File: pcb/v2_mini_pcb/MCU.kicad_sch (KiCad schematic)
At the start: 13 parts, among them SW1 SW_Push, SW2 SW_Push

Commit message: update pcb issues
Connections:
- net CHG_PG: now reaches U2.51 (GPIO40)
- no-connect marks 16 -> 15
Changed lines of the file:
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@@
-	)
-	(no_connect
-		(at 165.1 156.21)
 	)
 	(no_connect
@@
 	)
 	(bus_entry
+		(at 55.88 57.15)
+		(size -2.54 2.54)
+		(stroke
+			(width 0)
+			(type default)
+		)
+	)
+	(bus_entry
 		(at 119.38 62.23)
 		(size -2.54 2.54)
@@
 		)
 	)
+	(bus
+		(pts
+			(xy 55.88 52.07) (xy 55.88 57.15)
+		)
+		(stroke
+			(width 0)
+			(type default)
+		)
+	)
 	(wire
 		(pts
@@
 	(wire
 		(pts
+			(xy 53.34 59.69) (xy 38.1 59.69)
+		)
+		(stroke
+			(width 0)
+			(type default)
+		)
+	)
+	(wire
+		(pts
 			(xy 43.18 105.41) (xy 41.91 105.41)
 		)
@@
 		(pts
 			(xy 116.84 69.85) (xy 101.6 69.85)
+		)
+		(stroke
+			(width 0)
+			(type default)
+		)
+	)
+	(wire
+		(pts
+			(xy 165.1 156.21) (xy 181.61 156.21)
 		)
 		(stroke
@@
 		)
 	)
+	(label "CHG_PG"
+		(at 38.1 59.69 0)
+		(effects
+			(font
+				(size 1.27 1.27)
+			)
+			(justify left bottom)
+		)
+	)
 	(label "LCD_RN"
 		(at 194.31 34.29 0)
@@
 		(effects
 			(font
+				(size 1.27 1.27)
+			)
+			(justify right bottom)
+		)
+	)
+	(label "CHG_PG"
+		(at 181.61 156.21 180)
+		(effects
+			(font

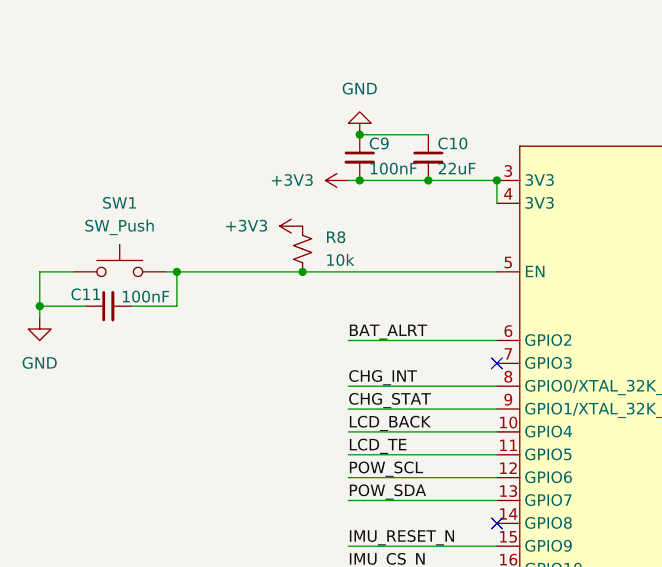
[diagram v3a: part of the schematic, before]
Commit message: ground to imu pins
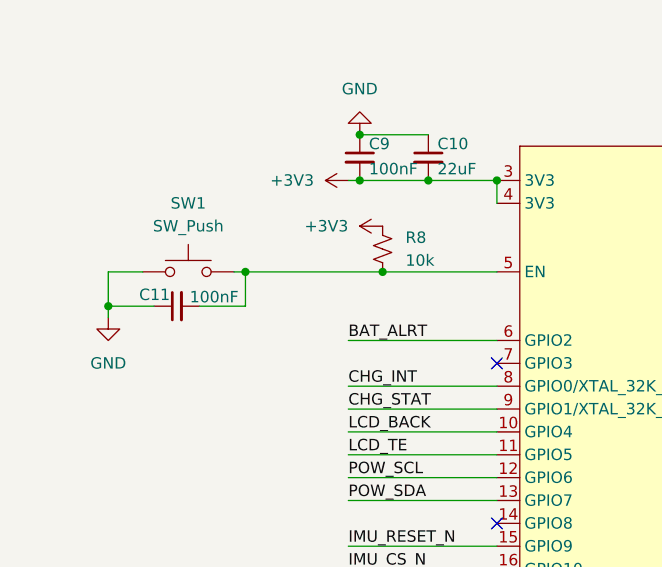
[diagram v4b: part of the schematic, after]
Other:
- moved on the sheet: C11, R8, SW1
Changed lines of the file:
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@@
 	(paper "A3")
 	(junction
-		(at 27.94 109.22)
+		(at 66.04 105.41)
 		(diameter 0)
 		(color 0 0 0 0)
 	)
 	(junction
-		(at 71.12 95.25)
+		(at 35.56 109.22)
 		(diameter 0)
 		(color 0 0 0 0)
 	)
 	(junction
-		(at 63.5 95.25)
+		(at 71.12 95.25)
 		(diameter 0)
 		(color 0 0 0 0)
 	)
 	(junction
-		(at 172.72 100.33)
+		(at 63.5 95.25)
 		(diameter 0)
 		(color 0 0 0 0)
 	)
 	(junction
-		(at 57.15 105.41)
+		(at 172.72 100.33)
 		(diameter 0)
 		(color 0 0 0 0)
@@
 	)
 	(junction
-		(at 43.18 105.41)
+		(at 50.8 105.41)
 		(diameter 0)
 		(color 0 0 0 0)
@@
 	(wire
 		(pts
-			(xy 27.94 109.22) (xy 27.94 105.41)
+			(xy 35.56 109.22) (xy 35.56 105.41)
 		)
 		(stroke
@@
 	(wire
 		(pts
-			(xy 43.18 109.22) (xy 43.18 105.41)
+			(xy 50.8 109.22) (xy 50.8 105.41)
 		)
 		(stroke
@@
 	(wire
 		(pts
-			(xy 43.18 105.41) (xy 57.15 105.41)
+			(xy 50.8 105.41) (xy 66.04 105.41)
 		)
 		(stroke
@@
 	(wire
 		(pts
-			(xy 27.94 110.49) (xy 27.94 109.22)
+			(xy 35.56 110.49) (xy 35.56 109.22)
 		)
 		(stroke
@@
 	(wire
 		(pts
-			(xy 38.1 109.22) (xy 43.18 109.22)
+			(xy 45.72 109.22) (xy 50.8 109.22)
 		)
 		(stroke
@@
 	(wire
 		(pts
-			(xy 43.18 105.41) (xy 41.91 105.41)
+			(xy 50.8 105.41) (xy 49.53 105.41)
 		)
 		(stroke
@@
 	(wire
 		(pts
-			(xy 27.94 109.22) (xy 33.02 109.22)
+			(xy 35.56 109.22) (xy 40.64 109.22)
 		)
 		(stroke
@@
 	(wire
 		(pts
-			(xy 27.94 105.41) (xy 31.75 105.41)
+			(xy 35.56 105.41) (xy 39.37 105.41)
 		)
 		(stroke
@@
 	(wire
 		(pts
-			(xy 86.36 44.45) (xy 71.12 44.45)
+			(xy 66.04 105.41) (xy 78.74 105.41)
 		)
 		(stroke
@@
 	(wire
 		(pts
-			(xy 132.08 49.53) (xy 152.4 49.53)
+			(xy 86.36 44.45) (xy 71.12 44.45)
 		)
 		(stroke
@@
 	(wire
 		(pts
-			(xy 62.23 118.11) (xy 78.74 118.11)
+			(xy 132.08 49.53) (xy 152.4 49.53)
 		)
 		(stroke
@@
 	(wire
 		(pts
-			(xy 57.15 105.41) (xy 78.74 105.41)
+			(xy 62.23 118.11) (xy 78.74 118.11)
 		)
 		(stroke
@@
 	(symbol
 		(lib_id "power:GND")
-		(at 27.94 110.49 0)
+		(at 35.56 110.49 0)
 		(unit 1)
 		(body_style 1)
@@
 		(fields_autoplaced yes)
 		(property "Reference" "#PWR059"
-			(at 27.94 116.84 0)
+			(at 35.56 116.84 0)
 			(hide yes)
 			(show_name no)
@@
 		)
 		(property "Value" "GND"
-			(at 27.94 115.57 0)
+			(at 35.56 115.57 0)
 			(show_name no)
 			(do_not_autoplace no)
@@
 		)
 		(property "Footprint" ""
-			(at 27.94 110.49 0)
+			(at 35.56 110.49 0)
 			(hide yes)
 			(show_name no)
@@
 		)
 		(property "Datasheet" ""
-			(at 27.94 110.49 0)
+			(at 35.56 110.49 0)
 			(hide yes)
 			(show_name no)
@@
 		)
 		(property "Description" "Power symbol creates a global label with name \"GND\" , ground"
-			(at 27.94 110.49 0)
+			(at 35.56 110.49 0)
 			(hide yes)
 			(show_name no)
@@
 	(symbol
 		(lib_id "Device:C_Small")
-		(at 35.56 109.22 90)
+		(at 43.18 109.22 90)
 		(unit 1)
 		(body_style 1)
@@
 		(dnp no)
 		(property "Reference" "C11"
-			(at 34.798 107.95 90)
+			(at 42.418 107.95 90)
 			(show_name no)
 			(do_not_autoplace no)
@@
 		)
 		(property "Value" "100nF"
-			(at 42.418 108.204 90)
+			(at 50.038 108.204 90)
 			(show_name no)
 			(do_not_autoplace no)
@@
 		)
 		(property "Footprint" ""
-			(at 35.56 109.22 0)
+			(at 43.18 109.22 0)
 			(hide yes)
 			(show_name no)
@@
 		)
 		(property "Datasheet" ""
-			(at 35.56 109.22 0)
+			(at 43.18 109.22 0)
 			(hide yes)
 			(show_name no)
@@
 		)
 		(property "Description" "Unpolarized capacitor, small symbol"
-			(at 35.56 109.22 0)
+			(at 43.18 109.22 0)
 			(hide yes)
 			(show_name no)
@@
 	(symbol
 		(lib_id "Switch:SW_Push")
-		(at 36.83 105.41 0)
+		(at 44.45 105.41 0)
 		(unit 1)
 		(body_style 1)
@@
 		(fields_autoplaced yes)
 		(property "Reference" "SW1"
-			(at 36.83 97.79 0)
+			(at 44.45 97.79 0)
 			(show_name no)
 			(do_not_autoplace no)
@@
 		)
 		(property "Value" "SW_Push"
-			(at 36.83 100.33 0)
+			(at 44.45 100.33 0)
 			(show_name no)
 			(do_not_autoplace no)
@@
 		)
 		(property "Footprint" ""
-			(at 36.83 100.33 0)
+			(at 44.45 100.33 0)
 			(hide yes)
 			(show_name no)
@@
 		)
 		(property "Datasheet" ""
-			(at 36.83 100.33 0)
+			(at 44.45 100.33 0)
 			(hide yes)
 			(show_name no)
@@
 		)
 		(property "Description" "Push button switch, generic, two pins"
-			(at 36.83 105.41 0)
+			(at 44.45 105.41 0)
 			(hide yes)
 			(show_name no)
@@
 	(symbol
 		(lib_id "power:+3V3")
-		(at 57.15 100.33 90)
+		(at 66.04 100.33 90)
 		(unit 1)
 		(body_style 1)
@@
 		(fields_autoplaced yes)
 		(property "Reference" "#PWR058"
-			(at 60.96 100.33 0)
+			(at 69.85 100.33 0)
 			(hide yes)
 			(show_name no)
@@
 		)
 		(property "Value" "+3V3"
-			(at 53.34 100.3299 90)
+			(at 62.23 100.3299 90)
 			(show_name no)
 			(do_not_autoplace no)
@@
 		)
 		(property "Footprint" ""
-			(at 57.15 100.33 0)
+			(at 66.04 100.33 0)
 			(hide yes)
 			(show_name no)
@@
 		)
 		(property "Datasheet" ""
-			(at 57.15 100.33 0)
+			(at 66.04 100.33 0)
 			(hide yes)
 			(show_name no)
@@
 		)
 		(property "Description" "Power symbol creates a global label with name \"+3V3\""
-			(at 57.15 100.33 0)
+			(at 66.04 100.33 0)
 			(hide yes)
 			(show_name no)
@@
 	(symbol
 		(lib_id "Device:R_Small_US")
-		(at 57.15 102.87 0)
+		(at 66.04 102.87 0)
 		(unit 1)
 		(body_style 1)
@@
 		(fields_autoplaced yes)
 		(property "Reference" "R8"
-			(at 59.69 101.5999 0)
+			(at 68.58 101.5999 0)
 			(show_name no)
 			(do_not_autoplace no)
@@
 		)
 		(property "Value" "10k"
-			(at 59.69 104.1399 0)
+			(at 68.58 104.1399 0)
 			(show_name no)
 			(do_not_autoplace no)
@@
 		)
 		(property "Footprint" ""
-			(at 57.15 102.87 0)
+			(at 66.04 102.87 0)
 			(hide yes)
 			(show_name no)
@@
 		)
 		(property "Datasheet" ""
-			(at 57.15 102.87 0)
+			(at 66.04 102.87 0)
 			(hide yes)
 			(show_name no)
@@
 		)
 		(property "Description" "Resistor, small US symbol"
-			(at 57.15 102.87 0)
+			(at 66.04 102.87 0)
 			(hide yes)
 			(show_name no)

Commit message: add mpn and footprints for some
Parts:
- added C12, C24: DNP, Capacitor_SMD:C_01005_0402Metric, symbol Device:C_Small
- added J5: TC2030, Connector:Tag-Connect_TC2030-IDC-NL_2x03_P1.27mm_Vertical, symbol Connector:TC2030
- added R30, R31: 22, symbol Device:R_Small_US
- C10: footprint (none) -> Capacitor_SMD:C_0201_0603Metric; MPN (none) -> CL10A226MQ8NRNC
- C11, C9: footprint (none) -> Capacitor_SMD:C_01005_0402Metric; MPN (none) -> CL05B104KB54PNC
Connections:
- net +3V3: now also J5.1
- net GND: now also C12.2, C24.2, J5.5
- net at R17.1: now also U2.41 (USB_DM); no longer U2.43 (GPIO34)
- net at U2.42 (GPIO33): now also R30.1; no longer R10.1
- net at U2.40 (USB_DP): now also R10.1
- net USB_VBUS_S: now reaches U2.44 (GPIO35)
- new net: R31.1, U2.43 (GPIO34)
- new net JTAG_DN: C24.1, J5.3, R30.2
- new net JTAG_DP: C12.1, J5.4, R31.2
- no-connect marks 15 -> 14
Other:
- moved on the sheet: R10, R17

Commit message: finish off mpn and footprints
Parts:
- C10: footprint Capacitor_SMD:C_0201_0603Metric -> Capacitor_SMD:C_0805_2012Metric; MPN CL10A226MQ8NRNC -> GRM21BR61A226ME44L
- C11, C9: footprint Capacitor_SMD:C_01005_0402Metric -> Capacitor_SMD:C_0402_1005Metric; MPN CL05B104KB54PNC -> GRM155R71C104KA88D
- C12, C24: footprint Capacitor_SMD:C_01005_0402Metric -> Capacitor_SMD:C_0402_1005Metric; MPN CL05A105KA5NQNC -> DNP
- J5: MPN (none) -> TC2030-IDC-NL (mating cable)
- R10, R17, R30, R31: footprint (none) -> Resistor_SMD:R_0402_1005Metric; MPN (none) -> 0402WGF220JTCE
- R18: footprint (none) -> Resistor_SMD:R_0402_1005Metric; MPN (none) -> RC0402FR-07499RL
- R8, R9: footprint (none) -> Resistor_SMD:R_0402_1005Metric; MPN (none) -> 0402WGF1002TCE
- SW1, SW2: footprint (none) -> Button_Switch_SMD:SW_SPST_B3U-1000P; MPN (none) -> B3U-1000P
- TP1, TP2: footprint (none) -> TestPoint:TestPoint_Pad_D1.0mm; MPN (none) -> N/A (PCB test pad)
- U2: footprint PCM_Espressif:ESP32-S31-WROOM-3 -> all:ESP32-S31-WROOM-3; MPN (none) -> ESP32-S31-WROOM-3-N16R16V
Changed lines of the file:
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@@
 			)
 		)
-		(property "Footprint" "Capacitor_SMD:C_01005_0402Metric"
+		(property "Footprint" "Capacitor_SMD:C_0402_1005Metric"
 			(at 340.36 88.9 0)
 			(hide yes)
@@
 			)
 		)
-		(property "MPN" "CL05A105KA5NQNC"
+		(property "MPN" "DNP"
 			(at 340.36 88.9 0)
 			(hide yes)
@@
 			)
 		)
-		(property "Footprint" "Capacitor_SMD:C_01005_0402Metric"
+		(property "Footprint" "Capacitor_SMD:C_0402_1005Metric"
 			(at 43.18 109.22 0)
 			(hide yes)
@@
 			)
 		)
-		(property "MPN" "CL05B104KB54PNC"
+		(property "MPN" "GRM155R71C104KA88D"
 			(at 43.18 109.22 90)
 			(hide yes)
@@
 			)
 		)
-		(property "Footprint" "Capacitor_SMD:C_0201_0603Metric"
+		(property "Footprint" "Capacitor_SMD:C_0805_2012Metric"
 			(at 71.12 92.71 0)
 			(hide yes)
@@
 			)
 		)
-		(property "MPN" "CL10A226MQ8NRNC"
+		(property "MPN" "GRM21BR61A226ME44L"
 			(at 71.12 92.71 0)
 			(hide yes)
@@
 			)
 		)
-		(property "Footprint" ""
+		(property "Footprint" "Button_Switch_SMD:SW_SPST_B3U-1000P"
 			(at 44.45 100.33 0)
 			(hide yes)
@@
 			)
 		)
-		(property "MPN" ""
+		(property "MPN" "B3U-1000P"
 			(at 44.45 105.41 0)
 			(hide yes)
@@
 			)
 		)
-		(property "Footprint" ""
+		(property "Footprint" "Resistor_SMD:R_0402_1005Metric"
 			(at 124.46 180.34 0)
 			(hide yes)
@@
 			)
 		)
-		(property "MPN" ""
+		(property "MPN" "0402WGF220JTCE"
 			(at 124.46 180.34 90)
 			(hide yes)
@@
 			)
 		)
-		(property "MPN" ""
+		(property "MPN" "TC2030-IDC-NL (mating cable)"
 			(at 323.85 86.36 0)
 			(hide yes)
@@
 			)
 		)
-		(property "Footprint" ""
+		(property "Footprint" "Resistor_SMD:R_0402_1005Metric"
 			(at 129.54 180.34 0)
 			(hide yes)
@@
 			)
 		)
-		(property "MPN" ""
+		(property "MPN" "0402WGF220JTCE"
 			(at 129.54 180.34 90)
 			(hide yes)
@@
 			)
 		)
-		(property "Footprint" ""
+		(property "Footprint" "Resistor_SMD:R_0402_1005Metric"
 			(at 127 180.34 0)
 			(hide yes)
@@
 			)
 		)
-		(property "MPN" ""
+		(property "MPN" "0402WGF220JTCE"
 			(at 127 180.34 90)
 			(hide yes)
@@
 			)
 		)
-		(property "Footprint" ""
+		(property "Footprint" "Resistor_SMD:R_0402_1005Metric"
 			(at 171.45 110.49 0)
 			(hide yes)
@@
 			)
 		)
-		(property "MPN" ""
+		(property "MPN" "RC0402FR-07499RL"
 			(at 171.45 110.49 90)
 			(hide yes)
@@
 			)
 		)
-		(property "Footprint" ""
+		(property "Footprint" "Resistor_SMD:R_0402_1005Metric"
 			(at 172.72 97.79 0)
 			(hide yes)
@@
 			)
 		)
-		(property "MPN" ""
+		(property "MPN" "0402WGF1002TCE"
 			(at 172.72 97.79 0)
 			(hide yes)
@@
 			)
 		)
-		(property "Footprint" "Capacitor_SMD:C_01005_0402Metric"
+		(property "Footprint" "Capacitor_SMD:C_0402_1005Metric"
 			(at 306.07 88.9 0)
 			(hide yes)
@@
 			)
 		)
-		(property "MPN" "CL05A105KA5NQNC"
+		(property "MPN" "DNP"
 			(at 306.07 88.9 0)
 			(hide yes)
@@
 			)
 		)
-		(property "Footprint" ""
+		(property "Footprint" "Button_Switch_SMD:SW_SPST_B3U-1000P"
 			(at 189.23 95.25 0)
 			(hide yes)
@@
 			)
 		)
-		(property "MPN" ""
+		(property "MPN" "B3U-1000P"
 			(at 189.23 100.33 0)
 			(hide yes)
@@
 			)
 		)
-		(property "Footprint" ""
+		(property "Footprint" "Resistor_SMD:R_0402_1005Metric"
 			(at 121.92 180.34 0)
 			(hide yes)
@@
 			)
 		)
-		(property "MPN" ""
+		(property "MPN" "0402WGF220JTCE"
 			(at 121.92 180.34 90)
 			(hide yes)
@@
 			)
 		)
-		(property "Footprint" ""
+		(property "Footprint" "Resistor_SMD:R_0402_1005Metric"
 			(at 66.04 102.87 0)
 			(hide yes)
@@
 			)
 		)
-		(property "MPN" ""
+		(property "MPN" "0402WGF1002TCE"
 			(at 66.04 102.87 0)
 			(hide yes)
@@
 			)
 		)
-		(property "Footprint" "Capacitor_SMD:C_01005_0402Metric"
+		(property "Footprint" "Capacitor_SMD:C_0402_1005Metric"
 			(at 63.5 92.71 0)
 			(hide yes)
@@
 			)
 		)
-		(property "MPN" "CL05B104KB54PNC"
+		(property "MPN" "GRM155R71C104KA88D"
 			(at 63.5 92.71 0)
 			(hide yes)
@@
 			)
 		)
-		(property "Footprint" ""
+		(property "Footprint" "TestPoint:TestPoint_Pad_D1.0mm"
 			(at 179.07 113.03 0)
 			(hide yes)
@@
 			)
 		)
-		(property "MPN" ""
+		(property "MPN" "N/A (PCB test pad)"
 			(at 179.07 107.95 90)
 			(hide yes)
@@
 			)
 		)
-		(property "Footprint" "PCM_Espressif:ESP32-S31-WROOM-3"
+		(property "Footprint" "all:ESP32-S31-WROOM-3"
 			(at 122.174 187.96 0)
 			(hide yes)
@@
 			)
 		)
-		(property "MPN" ""
+		(property "MPN" "ESP32-S31-WROOM-3-N16R16V"
 			(at 121.92 132.08 0)
 			(hide yes)
@@
 			)
 		)
-		(property "Footprint" ""
+		(property "Footprint" "TestPoint:TestPoint_Pad_D1.0mm"
 			(at 179.07 115.57 0)
 			(hide yes)
@@
 			)
 		)
-		(property "MPN" ""
+		(property "MPN" "N/A (PCB test pad)"
 			(at 179.07 110.49 90)
 			(hide yes)

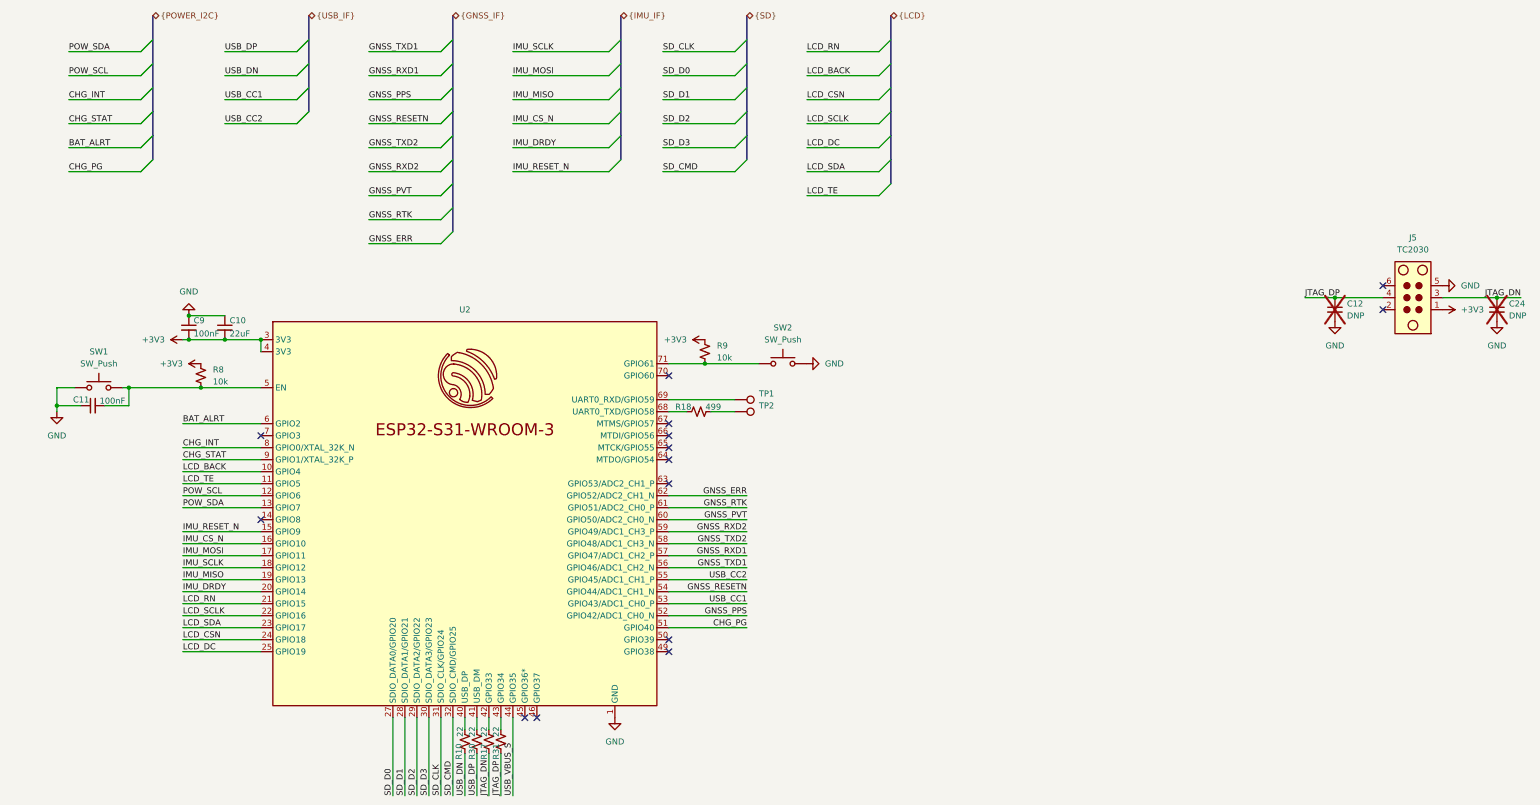
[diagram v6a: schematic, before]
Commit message: finish footprint matching
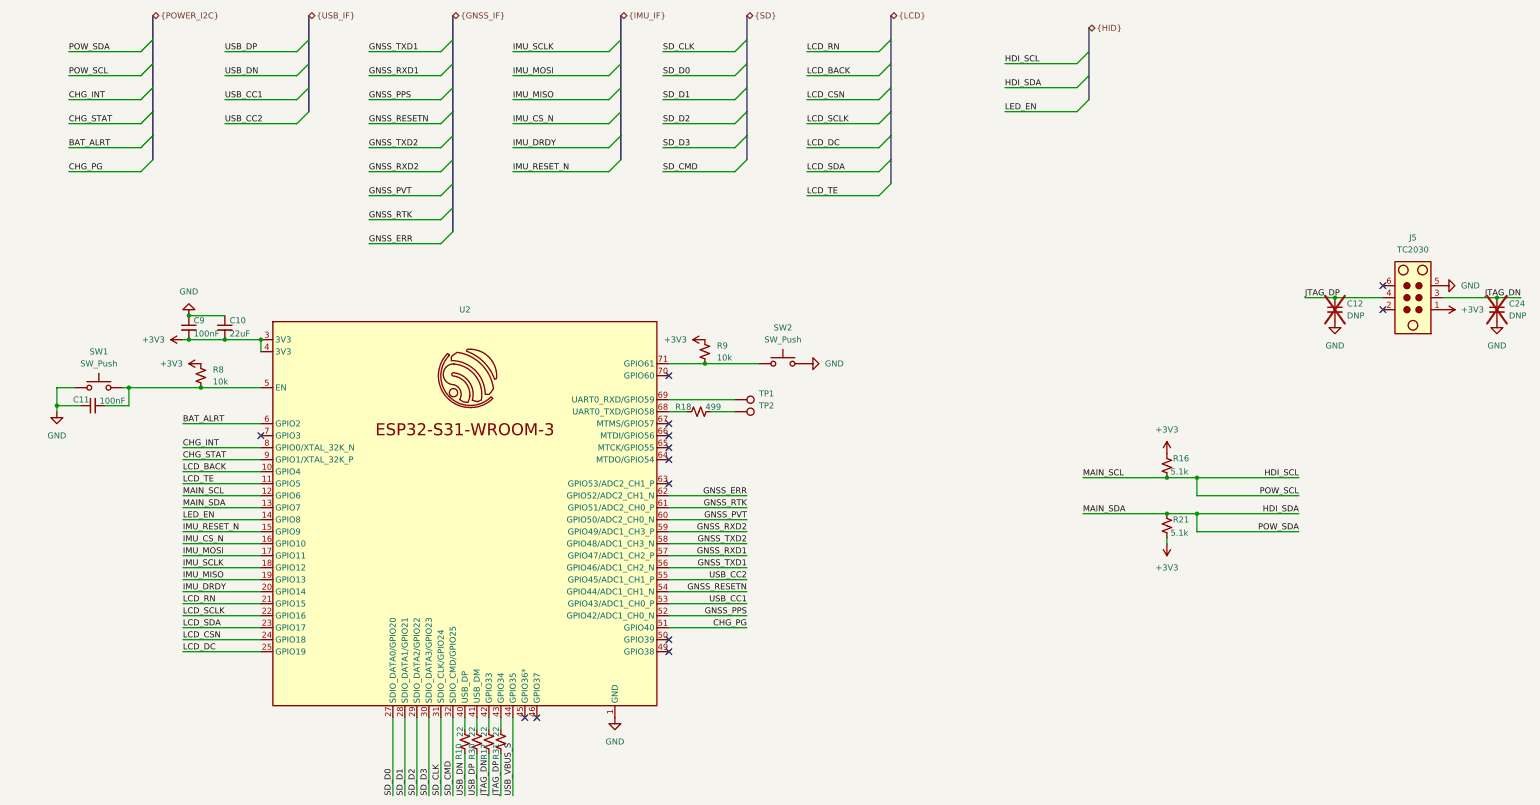
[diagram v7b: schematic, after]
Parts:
- added R16, R21: 5.1k, Resistor_SMD:R_0402_1005Metric, symbol Device:R_Small_US
- C10: Dielectric (none) -> X5R; JLCPCB_PN (none) -> C45783; LCSC (none) -> C45783; MPN GRM21BR61A226ME44L -> CL21A226MAQNNNE; Manufacturer (none) -> Samsung Electro-Mechanics; Supplier (none) -> JLCPCB Basic; Tolerance (none) -> 20%; Voltage (none) -> 25V
- C11, C9: Dielectric (none) -> X7R; JLCPCB_PN (none) -> C1525; LCSC (none) -> C1525; MPN GRM155R71C104KA88D -> CL05B104KO5NNNC; Manufacturer (none) -> Samsung Electro-Mechanics; Supplier (none) -> JLCPCB Basic; Tolerance (none) -> 10%; Voltage (none) -> 16V
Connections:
- net +3V3: now also R16.1, R21.2
- net LED_EN: now reaches U2.14 (GPIO8)
- net POW_SCL renamed HDI_SCL
- net HDI_SCL: now also R16.2
- net POW_SDA renamed HDI_SDA
- net HDI_SDA: now also R21.1
- no-connect marks 14 -> 13
